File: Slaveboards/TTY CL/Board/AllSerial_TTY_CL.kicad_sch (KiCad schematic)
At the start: 30 parts, among them Q2 BC857SMD, Q3 BC857SMD, Q4 BC857SMD, Q5 BC857SMD, Q6 BC857SMD, T4 BC847, X1 ALLSERIALSLAVE, X2 AKL18X-08W, X3 MA03-2W

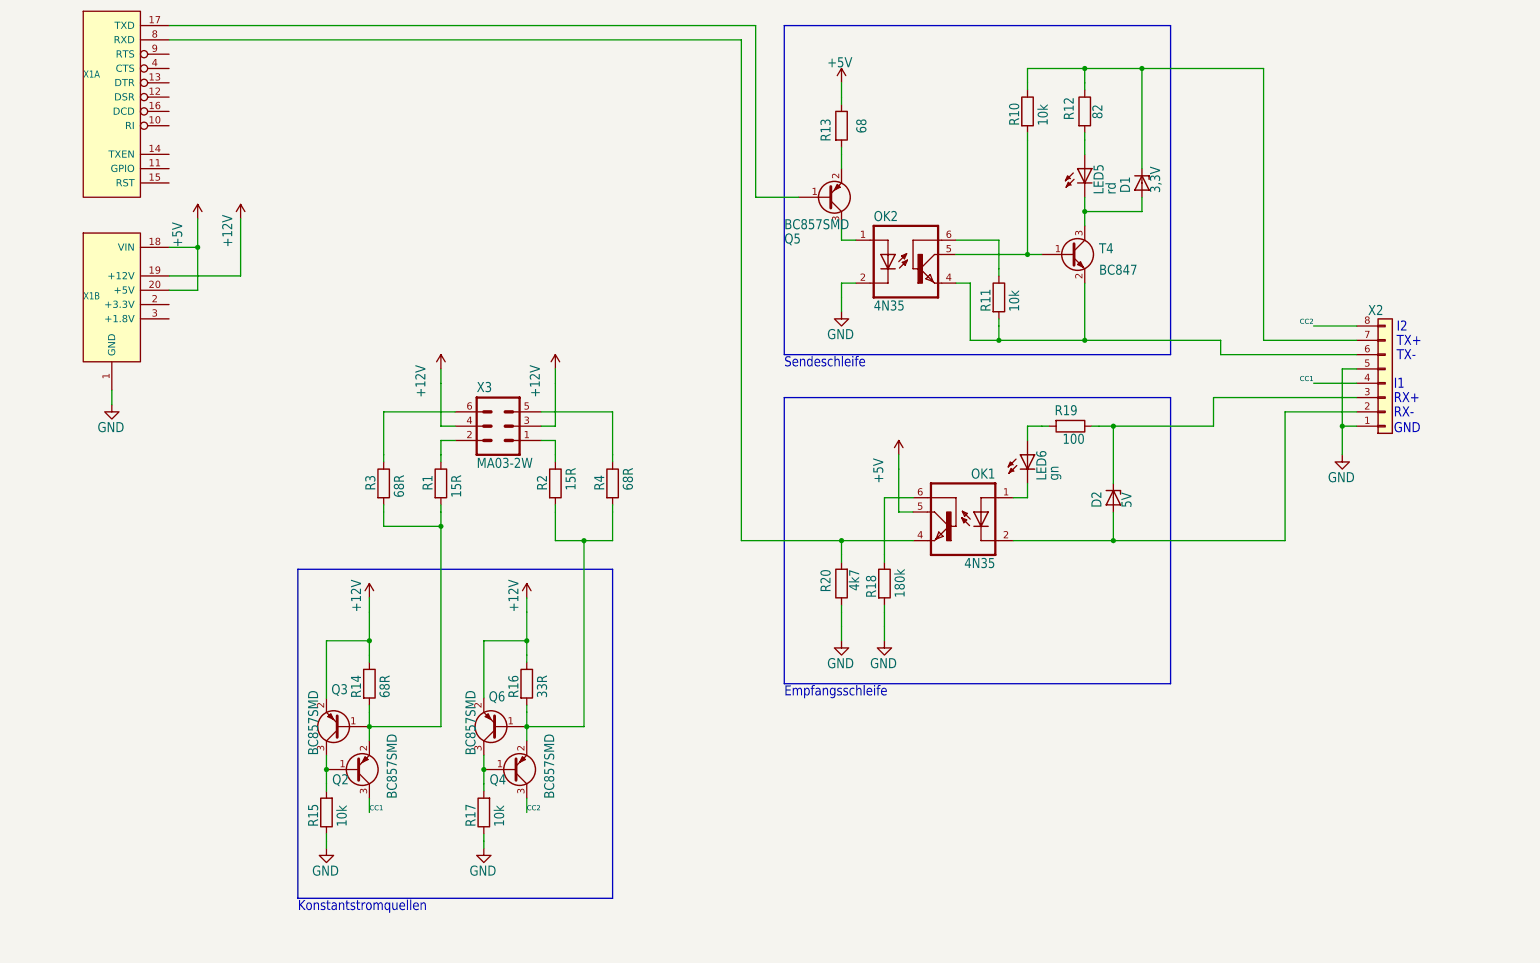
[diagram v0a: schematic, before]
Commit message: Update TTY CL slave board
Add ESP32 S3 WiFi MasterBoard
Update libs
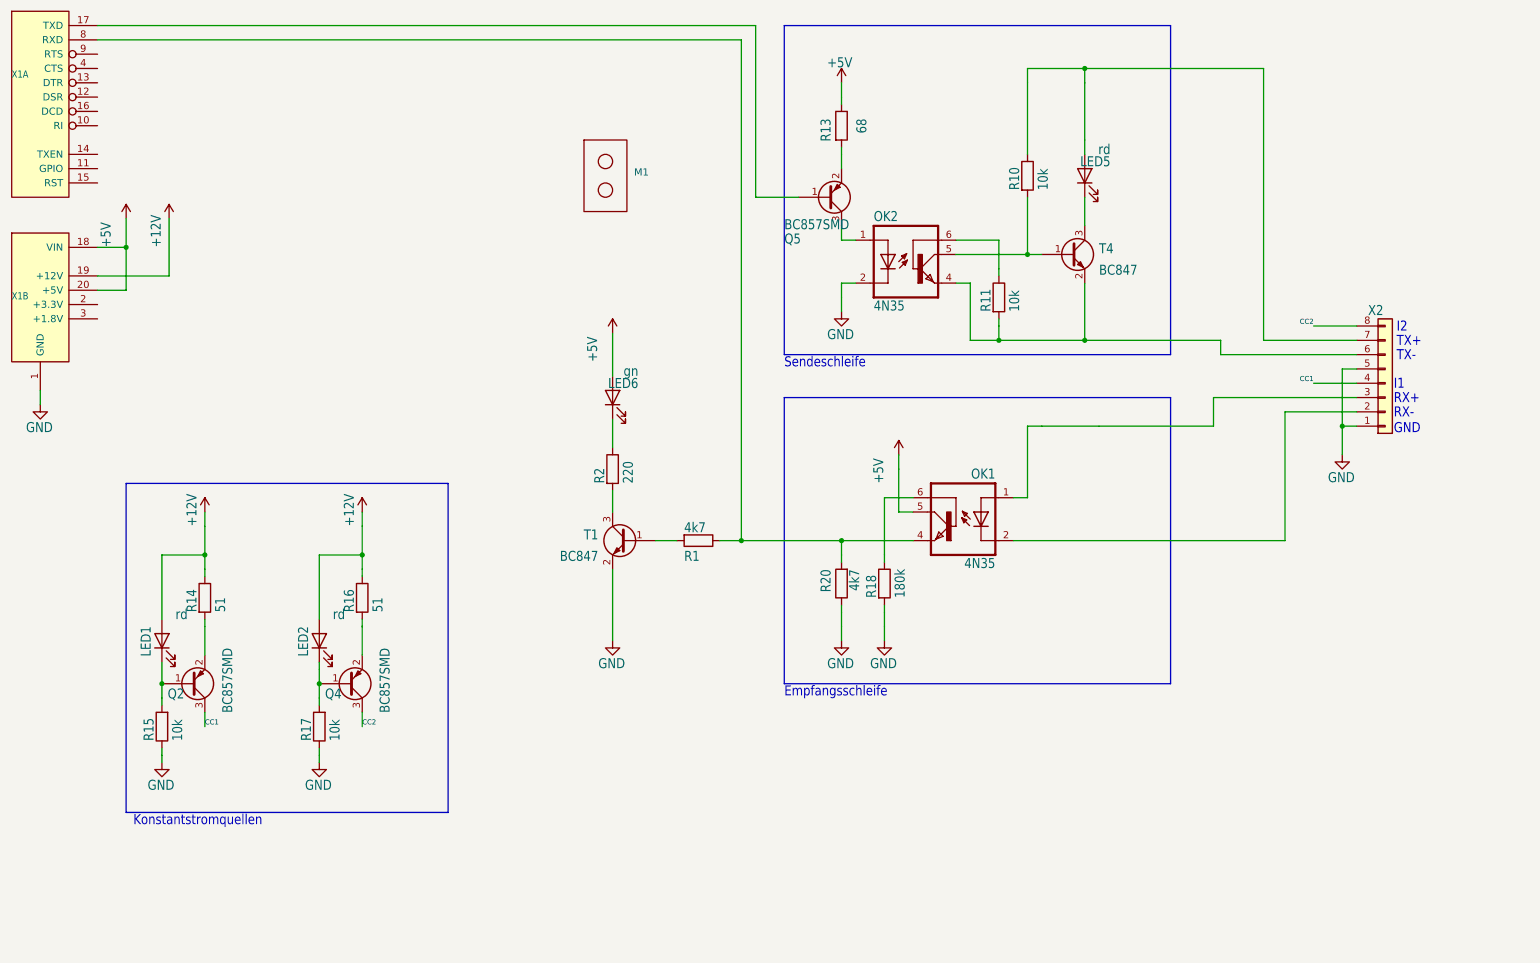
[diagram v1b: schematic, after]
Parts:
- removed D1: 3,3V, 5_TTY:SOT23, symbol 5_TTY-eagle-import:ZENER-DIODESOT23
- removed D2: 5V, 5_TTY:SOT23, symbol 5_TTY-eagle-import:ZENER-DIODESOT23
- removed Q3, Q6: BC857SMD, Package_TO_SOT_SMD:SOT-23, symbol Transistor_BJT:BC857
- removed R12: 82, Resistor_SMD:R_0805_2012Metric, symbol Device:R
- removed R19: 100, Resistor_SMD:R_0805_2012Metric, symbol Device:R
- removed R3, R4: 68R, Resistor_SMD:R_0805_2012Metric, symbol Device:R
- removed X3: MA03-2W, 5_TTY:MA03-2W, symbol 5_TTY-eagle-import:MA03-2W
- added LED1, LED2: rd, LED_SMD:LED_0603_1608Metric, symbol Device:LED
- added M1: ~, AllSerial:Mentor 1296.2012, symbol AllSerial:Mentor_1296.2012
- added T1: BC847, Package_TO_SOT_SMD:SOT-23, symbol Transistor_BJT:BC847
- LED5, LED6: footprint 5_TTY:CHIPLED_0603 -> LED_SMD:LED_0603_1608Metric; symbol 5_TTY-eagle-import:LEDCHIPLED_0603 -> Device:LED
- R1: value 15R -> 4k7; FARNELL 2498090 -> 2498050
- R14: value 68R -> 51; FARNELL 2498090 -> (none)
- R16: value 33R -> 51; FARNELL 2498090 -> (none)
- R2: value 15R -> 220
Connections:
- net +12V: now also LED1.2 (A), LED2.2 (A)
- net +5V: now also LED6.2 (A)
- net GND: now also T1.2 (E)
- net at Q2.2 (E), R14.2: no longer R1.2
- net at Q2.1 (B), R15.2: now also LED1.1 (K)
- net at OK1.4 (EMI), R20.2, X1.8 (RXD): now also R1.1
- net at T4.3 (C): now also LED5.1 (K); no longer LED5.C
- net at R10.1, X2.7 (Pin_7): now also LED5.2 (A)
- net at X2.3 (Pin_3): now also OK1.1 (A)
- net at R2.1: now also LED6.1 (K)
- net at Q4.2 (E), R16.2: no longer R2.2
- net at Q4.1 (B), R17.2: now also LED2.1 (K)
- new net: R1.2, T1.1 (B)
- new net: R2.2, T1.3 (C)
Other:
- moved on the sheet: Q2, Q4, R10, R14, R15, R16, R17, X1A, X1B

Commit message: Improve libraries
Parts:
- R13: value 68 -> 100
- R14, R16: value 51 -> 56
- R2: value 220 -> 180
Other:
- note added: "CC1"
- note added: "CC2"
- note added: "DUT"
- note added: "active"
- note added: "passive"
- moved on the sheet: LED1, LED2, LED5, LED6, M1, OK1, OK2, Q2, Q4, Q5, R1, R10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

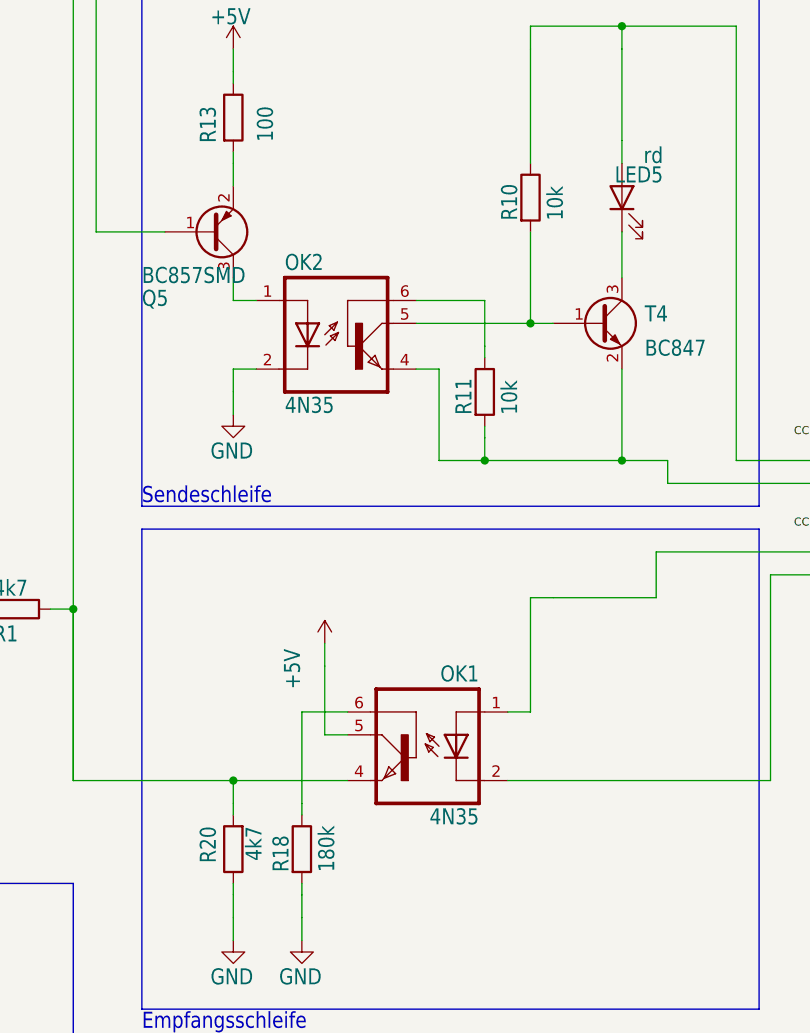
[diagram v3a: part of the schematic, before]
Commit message: Remove pads from cutouts
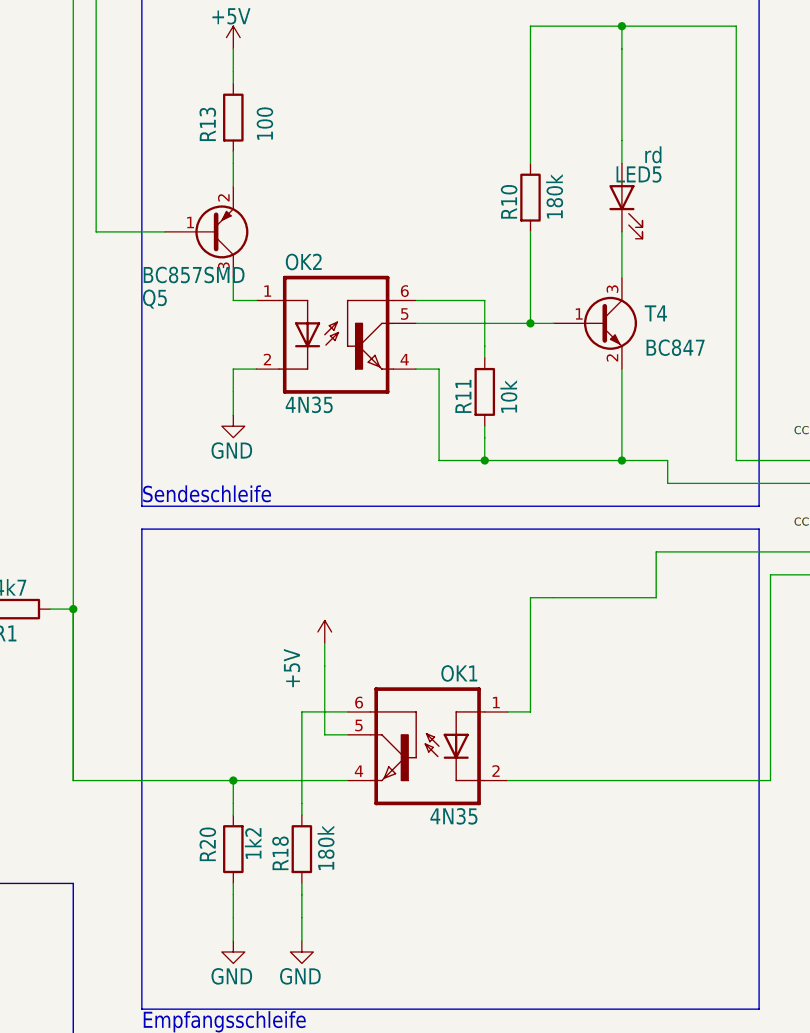
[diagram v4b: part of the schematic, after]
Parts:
- R10: value 10k -> 180k; FARNELL 2498051 -> (none)
- R20: value 4k7 -> 1k2; FARNELL 2498050 -> (none)
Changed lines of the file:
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@@
 			)
 		)
-		(property "Value" "10k"
+		(property "Value" "180k"
 			(at 129.54 59.69 90)
 			(effects
@@
 			)
 		)
-		(property "FARNELL" "2498051"
+		(property "FARNELL" ""
 			(at 125.73 57.15 0)
 			(effects
@@
 			)
 		)
-		(property "Value" "4k7"
+		(property "Value" "1k2"
 			(at 93.98 127 90)
 			(effects
@@
 			)
 		)
-		(property "FARNELL" "2498050"
+		(property "FARNELL" ""
 			(at 92.71 129.54 0)
 			(effects

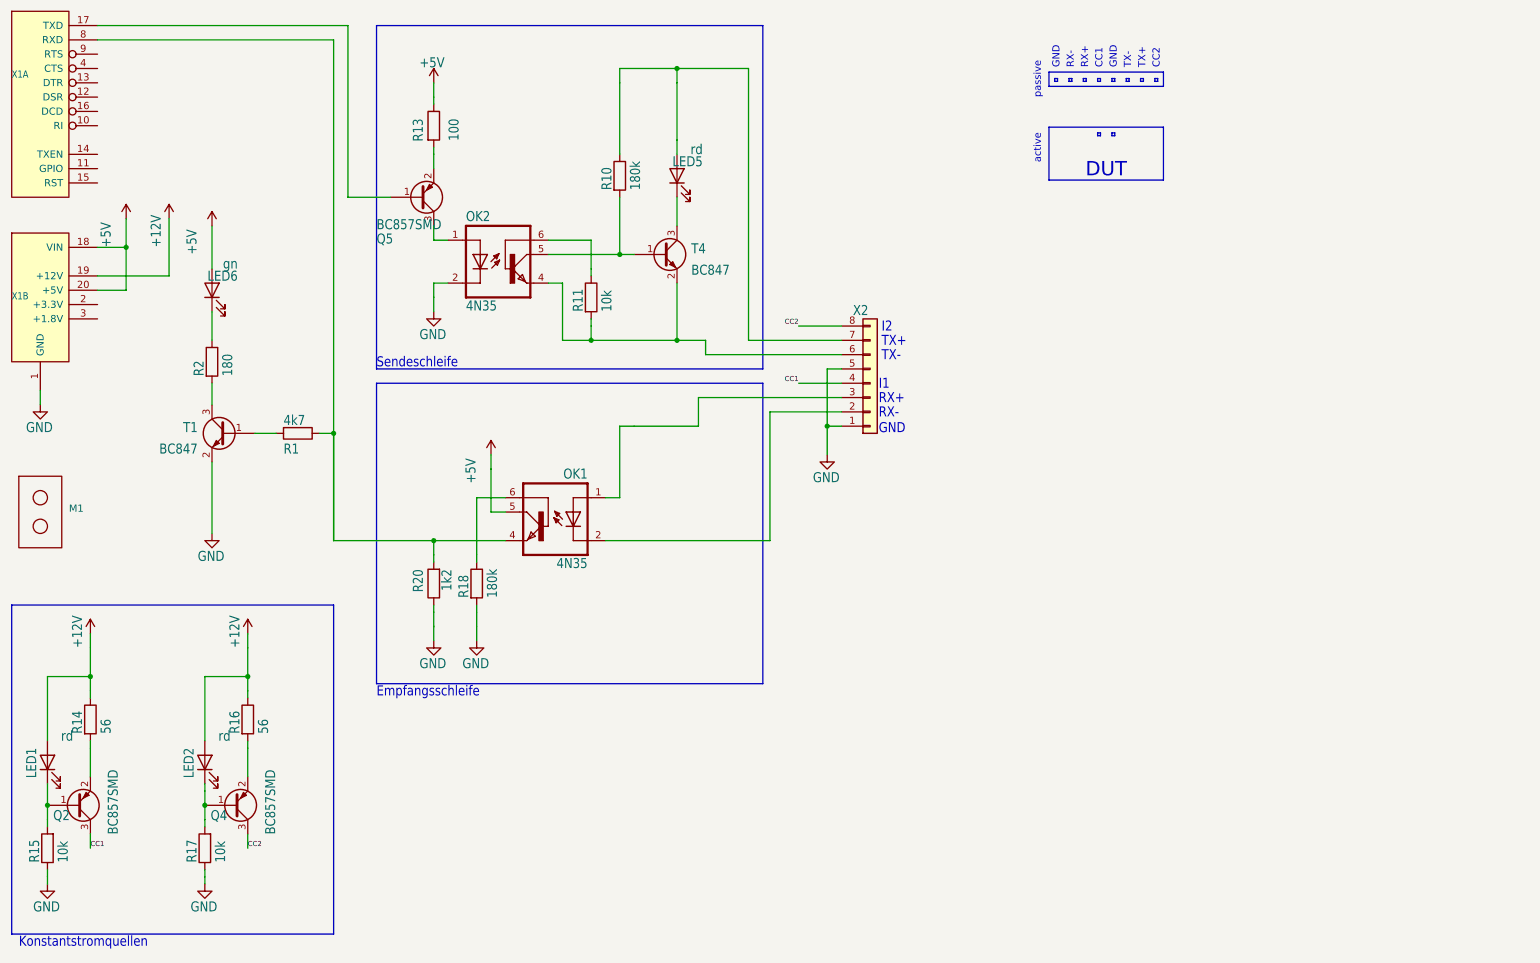
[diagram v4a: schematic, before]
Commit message: Add python testskript
Add mainboard tester
Add libraries
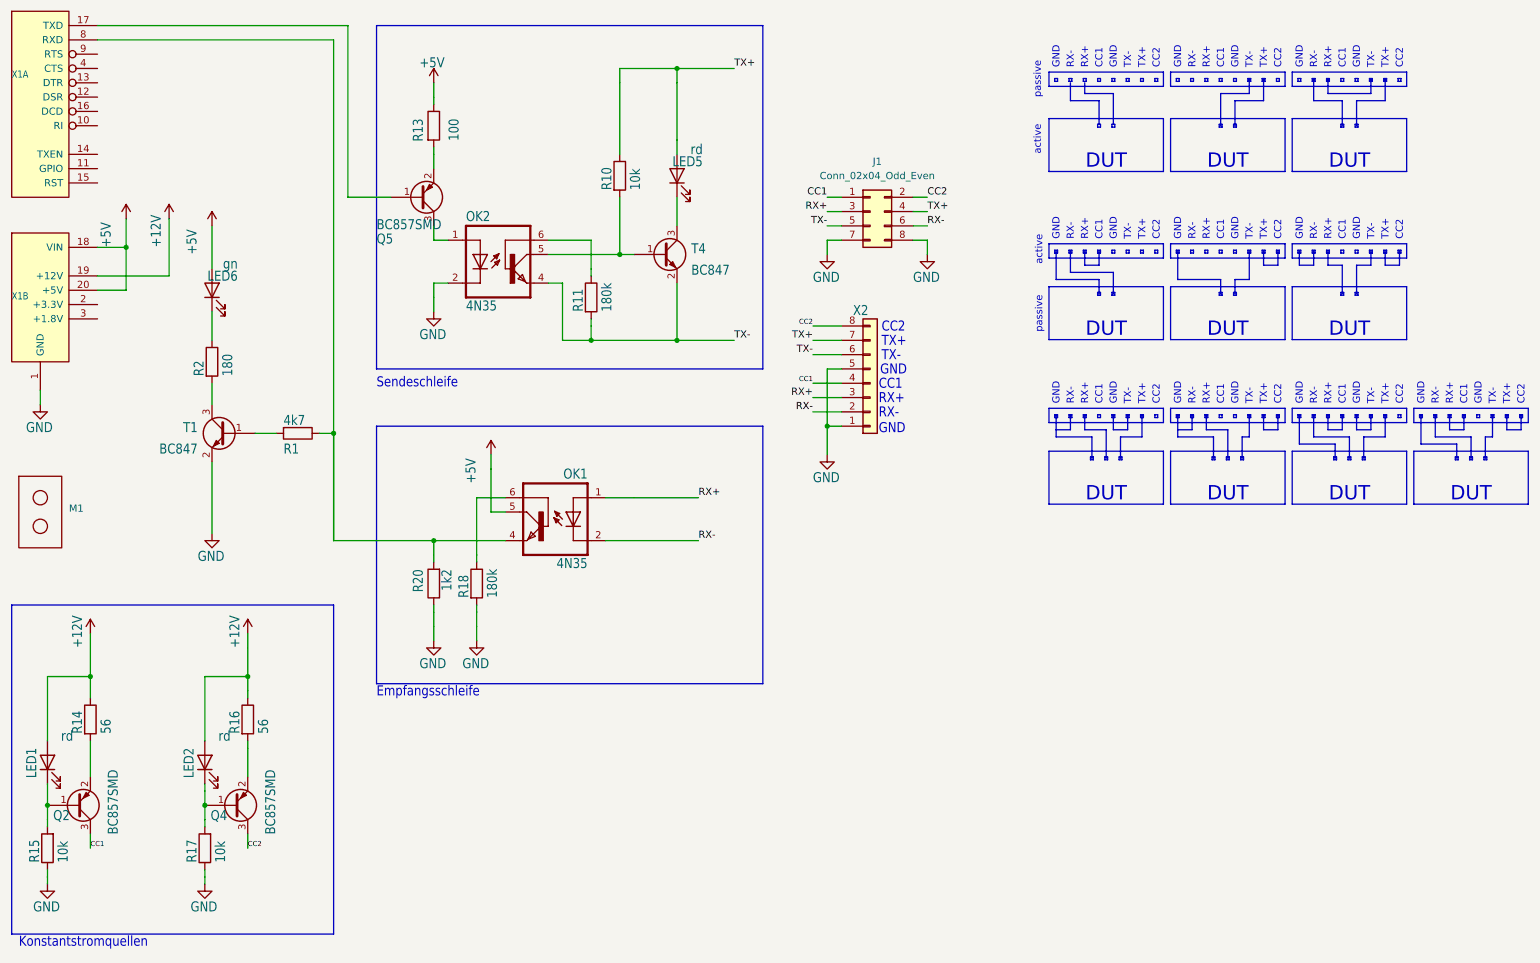
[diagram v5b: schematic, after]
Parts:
- added J1: Conn_02x04_Odd_Even, Connector_PinHeader_2.54mm:PinHeader_2x04_P2.54mm_Horizontal, symbol Connector_Generic:Conn_02x04_Odd_Even
- R10: value 180k -> 10k
- R11: value 10k -> 180k
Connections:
- net CC1: now also J1.1 (Pin_1)
- net CC2: now also J1.2 (Pin_2)
- net GND: now also J1.7 (Pin_7), J1.8 (Pin_8)
- net TX+: now reaches LED5.2 (A), R10.1, X2.7 (Pin_7)
- net TX+: now also J1.4 (Pin_4)
- net RX-: now reaches OK1.2 (C), X2.2 (Pin_2)
- net RX-: now also J1.6 (Pin_6)
- net RX+: now reaches OK1.1 (A), X2.3 (Pin_3)
- net RX+: now also J1.3 (Pin_3)
- net TX-: now reaches OK2.4 (EMI), R11.2, T4.2 (E), X2.6 (Pin_6)
- net TX-: now also J1.5 (Pin_5)
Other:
- note removed: "I1"
- note removed: "I2"

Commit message: add wiring schemes
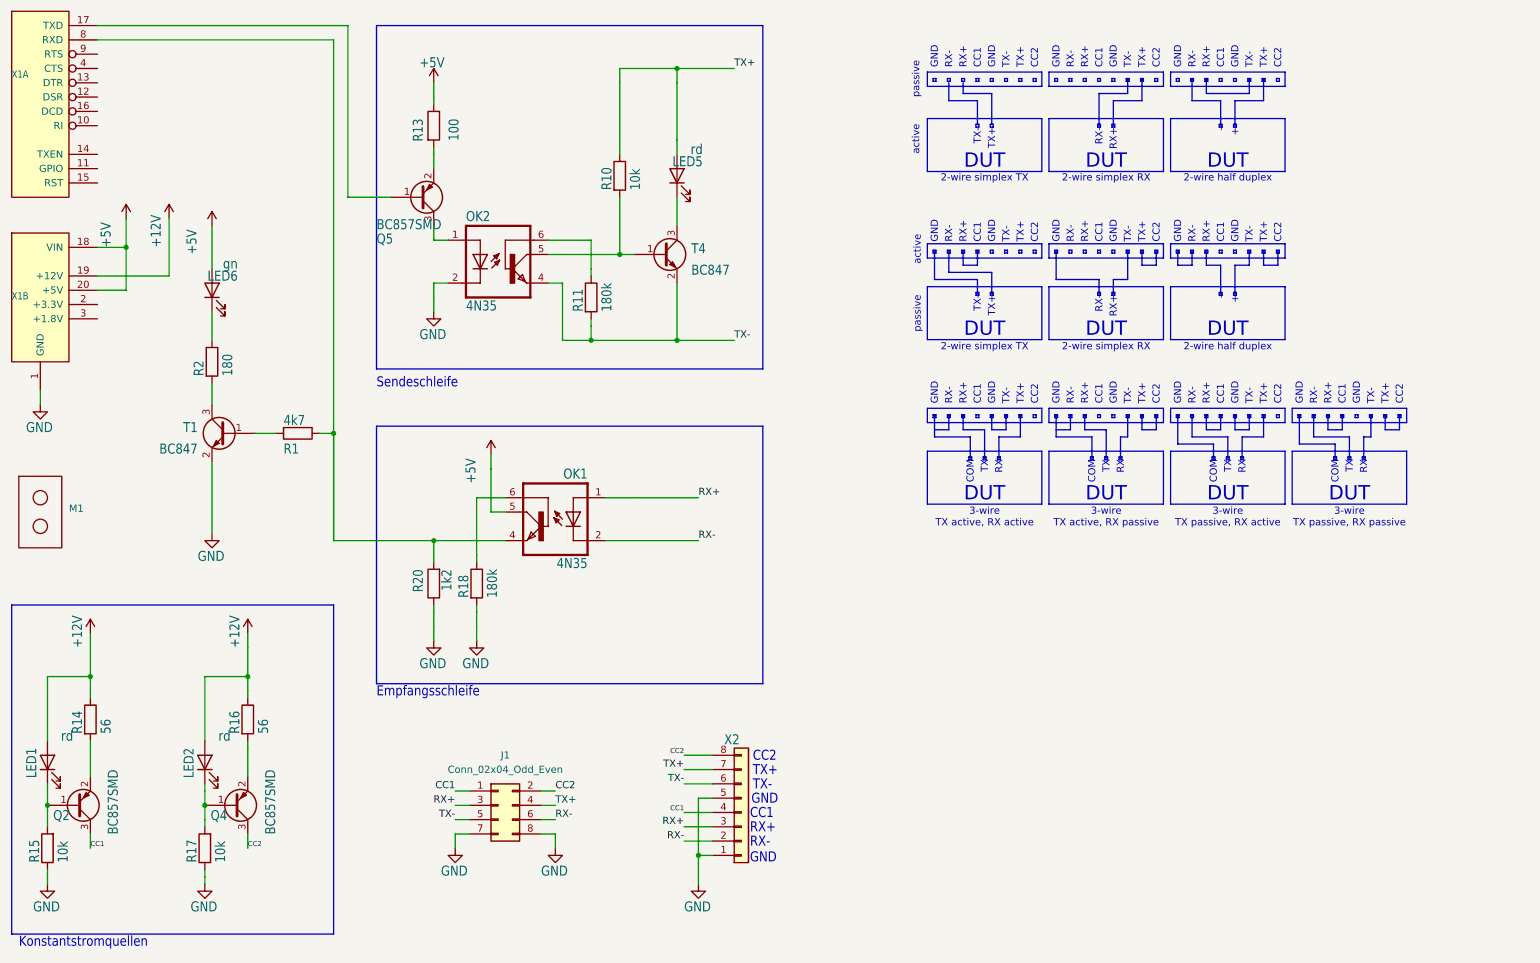
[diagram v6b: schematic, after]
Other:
- note added: "+"
- note added: "-"
- note added: "2-wire half duplex"
- note added: "2-wire simplex RX"
- note added: "2-wire simplex TX"
- note added: "3-wire TX active, RX active"
- note added: "3-wire TX active, RX passive"
- note added: "3-wire TX passive, RX active"
- note added: "3-wire TX passive, RX passive"
- note added: "COM"
- note added: "RX"
- note added: "TX"
- moved on the sheet: J1, X2
